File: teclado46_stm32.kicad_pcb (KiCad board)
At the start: 2 copper layers, 9 parts, among them U1 XC6206PxxxMR, U2 STM32G474CETx

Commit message: chore: add keyboard switches
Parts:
- added C14: 1u, Capacitor_SMD:C_0402_1005Metric, B.Cu at (105.9, 239.0)
- added D1: 1N4148W, Diode_SMD:D_SOD-123, B.Cu at (-143.7, 193.2)
- added D10: 1N4148W, Diode_SMD:D_SOD-123, B.Cu at (-143.7, 223.3)
- added D11: 1N4148W, Diode_SMD:D_SOD-123, B.Cu at (-149.5, 193.2)
- added D12: 1N4148W, Diode_SMD:D_SOD-123, B.Cu at (-149.5, 196.6)
- added D13: 1N4148W, Diode_SMD:D_SOD-123, B.Cu at (-149.5, 199.9)
- added D14: 1N4148W, Diode_SMD:D_SOD-123, B.Cu at (-149.5, 203.2)
- added D15: 1N4148W, Diode_SMD:D_SOD-123, B.Cu at (-149.5, 206.6)
- added D16: 1N4148W, Diode_SMD:D_SOD-123, B.Cu at (-149.5, 209.9)
- added D17: 1N4148W, Diode_SMD:D_SOD-123, B.Cu at (-149.5, 213.3)
- added D18: 1N4148W, Diode_SMD:D_SOD-123, B.Cu at (-149.5, 216.7)
- added D19: 1N4148W, Diode_SMD:D_SOD-123, B.Cu at (-149.5, 220.0)
- added D2: 1N4148W, Diode_SMD:D_SOD-123, B.Cu at (-143.7, 196.6)
- added D20: 1N4148W, Diode_SMD:D_SOD-123, B.Cu at (-149.5, 223.3)
- added D21: 1N4148W, Diode_SMD:D_SOD-123, B.Cu at (-155.3, 193.2)
- added D22: 1N4148W, Diode_SMD:D_SOD-123, B.Cu at (-155.3, 196.6)
- added D23: 1N4148W, Diode_SMD:D_SOD-123, B.Cu at (-155.3, 199.9)
- added D24: 1N4148W, Diode_SMD:D_SOD-123, B.Cu at (-155.3, 203.2)
- added D25: 1N4148W, Diode_SMD:D_SOD-123, B.Cu at (-155.3, 206.6)
- added D26: 1N4148W, Diode_SMD:D_SOD-123, B.Cu at (-155.3, 209.9)
- added D27: 1N4148W, Diode_SMD:D_SOD-123, B.Cu at (-155.3, 213.3)
- added D28: 1N4148W, Diode_SMD:D_SOD-123, B.Cu at (-155.3, 216.7)
- added D29: 1N4148W, Diode_SMD:D_SOD-123, B.Cu at (-155.3, 220.0)
- added D3: 1N4148W, Diode_SMD:D_SOD-123, B.Cu at (-143.7, 199.9)
- added D30: 1N4148W, Diode_SMD:D_SOD-123, B.Cu at (-155.3, 223.3)
- added D31: 1N4148W, Diode_SMD:D_SOD-123, B.Cu at (-161.1, 193.2)
- added D32: 1N4148W, Diode_SMD:D_SOD-123, B.Cu at (-161.1, 196.6)
- added D33: 1N4148W, Diode_SMD:D_SOD-123, B.Cu at (-161.1, 199.9)
- added D34: 1N4148W, Diode_SMD:D_SOD-123, B.Cu at (-161.1, 203.2)
- added D35: 1N4148W, Diode_SMD:D_SOD-123, B.Cu at (-161.1, 206.6)
- added D36: 1N4148W, Diode_SMD:D_SOD-123, B.Cu at (-161.1, 209.9)
- added D37: 1N4148W, Diode_SMD:D_SOD-123, B.Cu at (-161.1, 213.3)
- added D38: 1N4148W, Diode_SMD:D_SOD-123, B.Cu at (-161.1, 216.7)
- added D39: 1N4148W, Diode_SMD:D_SOD-123, B.Cu at (-161.1, 220.0)
- added D4: 1N4148W, Diode_SMD:D_SOD-123, B.Cu at (-143.7, 203.2)
- added D40: 1N4148W, Diode_SMD:D_SOD-123, B.Cu at (-161.1, 223.3)
- added D41: 1N4148W, Diode_SMD:D_SOD-123, B.Cu at (-166.9, 193.2)
- added D42: 1N4148W, Diode_SMD:D_SOD-123, B.Cu at (-166.9, 196.6)
- added D43: 1N4148W, Diode_SMD:D_SOD-123, B.Cu at (-166.9, 199.9)
- added D44: 1N4148W, Diode_SMD:D_SOD-123, B.Cu at (-166.9, 203.2)
- added D45: 1N4148W, Diode_SMD:D_SOD-123, B.Cu at (-166.9, 206.6)
- added D46: 1N4148W, Diode_SMD:D_SOD-123, B.Cu at (-166.9, 209.9)
- added D5: 1N4148W, Diode_SMD:D_SOD-123, B.Cu at (-143.7, 206.6)
- added D6: 1N4148W, Diode_SMD:D_SOD-123, B.Cu at (-143.7, 209.9)
- added D7: 1N4148W, Diode_SMD:D_SOD-123, B.Cu at (-143.7, 213.3)
- added D8: 1N4148W, Diode_SMD:D_SOD-123, B.Cu at (-143.7, 216.7)
- added D9: 1N4148W, Diode_SMD:D_SOD-123, B.Cu at (-143.7, 220.0)
- added MX1: MX_SW_HS, PCM_marbastlib-mx:SW_MX_HS_CPG151101S11_1u, B.Cu at (-45.8, 199.1)
- added MX10: MX_SW_HS, PCM_marbastlib-mx:SW_MX_HS_CPG151101S11_1u, B.Cu at (-63.0, 214.1)
- added MX11: MX_SW_HS, PCM_marbastlib-mx:SW_MX_HS_CPG151101S11_1u, B.Cu at (-63.0, 229.2)
- added MX12: MX_SW_HS, PCM_marbastlib-mx:SW_MX_HS_CPG151101S11_1u, B.Cu at (-63.0, 244.2)
- added MX13: MX_SW_HS, PCM_marbastlib-mx:SW_MX_HS_CPG151101S11_1u, B.Cu at (-63.0, 259.2)
- added MX14: MX_SW_HS, PCM_marbastlib-mx:SW_MX_HS_CPG151101S11_1u, B.Cu at (-63.0, 274.3)
- added MX15: MX_SW_HS, PCM_marbastlib-mx:SW_MX_HS_CPG151101S11_1u, B.Cu at (-63.0, 289.4)
- added MX16: MX_SW_HS, PCM_marbastlib-mx:SW_MX_HS_CPG151101S11_1u, B.Cu at (-63.0, 304.4)
- added MX17: MX_SW_HS, PCM_marbastlib-mx:SW_MX_HS_CPG151101S11_1u, B.Cu at (-80.1, 199.1)
- added MX18: MX_SW_HS, PCM_marbastlib-mx:SW_MX_HS_CPG151101S11_1u, B.Cu at (-80.1, 214.1)
- added MX19: MX_SW_HS, PCM_marbastlib-mx:SW_MX_HS_CPG151101S11_1u, B.Cu at (-80.1, 229.2)
- added MX2: MX_SW_HS, PCM_marbastlib-mx:SW_MX_HS_CPG151101S11_1u, B.Cu at (-45.8, 214.1)
- added MX20: MX_SW_HS, PCM_marbastlib-mx:SW_MX_HS_CPG151101S11_1u, B.Cu at (-80.1, 244.2)
- added MX21: MX_SW_HS, PCM_marbastlib-mx:SW_MX_HS_CPG151101S11_1u, B.Cu at (-80.1, 259.2)
- added MX22: MX_SW_HS, PCM_marbastlib-mx:SW_MX_HS_CPG151101S11_1u, B.Cu at (-80.1, 274.3)
- added MX23: MX_SW_HS, PCM_marbastlib-mx:SW_MX_HS_CPG151101S11_1u, B.Cu at (-80.1, 289.4)
- added MX24: MX_SW_HS, PCM_marbastlib-mx:SW_MX_HS_CPG151101S11_1u, B.Cu at (-80.1, 304.4)
- added MX25: MX_SW_HS, PCM_marbastlib-mx:SW_MX_HS_CPG151101S11_1u, B.Cu at (-97.3, 199.1)
- added MX26: MX_SW_HS, PCM_marbastlib-mx:SW_MX_HS_CPG151101S11_1u, B.Cu at (-97.3, 214.1)
- added MX27: MX_SW_HS, PCM_marbastlib-mx:SW_MX_HS_CPG151101S11_1u, B.Cu at (-97.3, 229.2)
- added MX28: MX_SW_HS, PCM_marbastlib-mx:SW_MX_HS_CPG151101S11_1u, B.Cu at (-97.3, 244.2)
- added MX29: MX_SW_HS, PCM_marbastlib-mx:SW_MX_HS_CPG151101S11_1u, B.Cu at (-97.3, 259.2)
- added MX3: MX_SW_HS, PCM_marbastlib-mx:SW_MX_HS_CPG151101S11_1u, B.Cu at (-45.8, 229.2)
- added MX30: MX_SW_HS, PCM_marbastlib-mx:SW_MX_HS_CPG151101S11_1u, B.Cu at (-97.3, 274.3)
- added MX31: MX_SW_HS, PCM_marbastlib-mx:SW_MX_HS_CPG151101S11_1u, B.Cu at (-97.3, 289.4)
- added MX32: MX_SW_HS, PCM_marbastlib-mx:SW_MX_HS_CPG151101S11_1u, B.Cu at (-97.3, 304.4)
- added MX33: MX_SW_HS, PCM_marbastlib-mx:SW_MX_HS_CPG151101S11_1u, B.Cu at (-114.4, 199.1)
- added MX34: MX_SW_HS, PCM_marbastlib-mx:SW_MX_HS_CPG151101S11_1u, B.Cu at (-114.4, 214.1)
- added MX35: MX_SW_HS, PCM_marbastlib-mx:SW_MX_HS_CPG151101S11_1u, B.Cu at (-114.4, 229.2)
- added MX36: MX_SW_HS, PCM_marbastlib-mx:SW_MX_HS_CPG151101S11_1u, B.Cu at (-114.4, 244.2)
- added MX37: MX_SW_HS, PCM_marbastlib-mx:SW_MX_HS_CPG151101S11_1u, B.Cu at (-114.4, 259.2)
- added MX38: MX_SW_HS, PCM_marbastlib-mx:SW_MX_HS_CPG151101S11_1u, B.Cu at (-114.4, 274.3)
- added MX39: MX_SW_HS, PCM_marbastlib-mx:SW_MX_HS_CPG151101S11_1u, B.Cu at (-114.4, 289.4)
- added MX4: MX_SW_HS, PCM_marbastlib-mx:SW_MX_HS_CPG151101S11_1u, B.Cu at (-45.8, 244.2)
- added MX40: MX_SW_HS, PCM_marbastlib-mx:SW_MX_HS_CPG151101S11_1u, B.Cu at (-114.4, 304.4)
- added MX41: MX_SW_HS, PCM_marbastlib-mx:SW_MX_HS_CPG151101S11_1u, B.Cu at (-131.6, 199.1)
- added MX42: MX_SW_HS, PCM_marbastlib-mx:SW_MX_HS_CPG151101S11_1u, B.Cu at (-131.6, 214.1)
- added MX43: MX_SW_HS, PCM_marbastlib-mx:SW_MX_HS_CPG151101S11_1u, B.Cu at (-131.6, 229.2)
- added MX44: MX_SW_HS, PCM_marbastlib-mx:SW_MX_HS_CPG151101S11_1u, B.Cu at (-131.6, 244.2)
- added MX45: MX_SW_HS, PCM_marbastlib-mx:SW_MX_HS_CPG151101S11_1u, B.Cu at (-131.6, 259.2)
- added MX46: MX_SW_HS, PCM_marbastlib-mx:SW_MX_HS_CPG151101S11_1u, B.Cu at (-131.6, 274.3)
- added MX5: MX_SW_HS, PCM_marbastlib-mx:SW_MX_HS_CPG151101S11_1u, B.Cu at (-45.8, 259.2)
- added MX6: MX_SW_HS, PCM_marbastlib-mx:SW_MX_HS_CPG151101S11_1u, B.Cu at (-45.8, 274.3)
- added MX7: MX_SW_HS, PCM_marbastlib-mx:SW_MX_HS_CPG151101S11_1u, B.Cu at (-45.8, 289.4)
- added MX8: MX_SW_HS, PCM_marbastlib-mx:SW_MX_HS_CPG151101S11_1u, B.Cu at (-45.8, 304.4)
- added MX9: MX_SW_HS, PCM_marbastlib-mx:SW_MX_HS_CPG151101S11_1u, B.Cu at (-63.0, 199.1)
- added U4: W25Q128JVS, Package_SO:SOIC-8_5.3x5.3mm_P1.27mm, B.Cu at (105.7, 230.9)
- moved C3 109.1 mm to (159.9, 247.8)
- moved U1 109.1 mm to (165.4, 231.6)
- moved C6 109.1 mm to (147.8, 238.9)
- moved C7 109.1 mm to (147.8, 240.8)
- moved U2 109.1 mm to (133.2, 223.1)
- moved C1 109.1 mm to (161.4, 230.2)
- moved C2 109.1 mm to (161.4, 232.2)
- moved C4 109.1 mm to (147.8, 234.9)
- moved C5 109.1 mm to (147.8, 236.9)
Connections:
- U2 pad 14: unconnected-(U2-PA6-Pad14) -> Q_103
- U2 pad 15: unconnected-(U2-PA7-Pad15) -> Q_102
- U2 pad 16: unconnected-(U2-PB0-Pad16) -> Q_101
- U2 pad 17: unconnected-(U2-PB1-Pad17) -> Q_100
- U2 pad 22: unconnected-(U2-PB10-Pad22) -> Q_CLK
- U2 pad 25: unconnected-(U2-PB11-Pad25) -> Q_SEL

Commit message: chore: routed caps, flash and regulator
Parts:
- moved D36 428.0 mm to (244.5, 73.0), turned to 90 degrees
- moved D46 427.9 mm to (244.5, 92.1), turned to 90 degrees
- moved D24 426.7 mm to (244.5, 54.0), turned to 90 degrees
- moved D12 425.8 mm to (244.5, 34.9), turned to 90 degrees
- moved MX46 416.4 mm to (241.3, 88.9)
- moved MX24 409.4 mm to (241.3, 50.8)
- moved D35 408.9 mm to (225.4, 73.0), turned to 90 degrees
- moved D45 408.7 mm to (225.4, 92.1), turned to 90 degrees
- moved D23 407.7 mm to (225.4, 54.0), turned to 90 degrees
- moved D11 407.0 mm to (225.4, 34.9), turned to 90 degrees
- moved D10 397.6 mm to (206.4, 34.9), turned to 90 degrees
- moved MX36 396.1 mm to (241.3, 69.8)
- moved MX45 392.7 mm to (222.2, 88.9)
- moved D34 389.8 mm to (206.4, 73.0), turned to 90 degrees
- moved D44 389.5 mm to (206.4, 92.1), turned to 90 degrees
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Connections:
- C3 pad 1: +3.3V -> +3V3
- C4 pad 1: +3.3V -> +3V3
- C5 pad 1: +3.3V -> +3V3
- C6 pad 1: +3.3V -> +3V3
- C7 pad 1: +3.3V -> +3V3
- D1 pad 1: unconnected-(D1-K-Pad1) -> ROW 0
- D10 pad 1: unconnected-(D10-K-Pad1) -> ROW 0
- D11 pad 1: unconnected-(D11-K-Pad1) -> ROW 0
- D12 pad 1: unconnected-(D12-K-Pad1) -> ROW 0
- D13 pad 1: unconnected-(D13-K-Pad1) -> ROW 1
- D14 pad 1: unconnected-(D14-K-Pad1) -> ROW 1
- D15 pad 1: unconnected-(D15-K-Pad1) -> ROW 1
- D16 pad 1: unconnected-(D16-K-Pad1) -> ROW 1
- D17 pad 1: unconnected-(D17-K-Pad1) -> ROW 1
- D18 pad 1: unconnected-(D18-K-Pad1) -> ROW 1
- D19 pad 1: unconnected-(D19-K-Pad1) -> ROW 1
- D2 pad 1: unconnected-(D2-K-Pad1) -> ROW 0
- D20 pad 1: unconnected-(D20-K-Pad1) -> ROW 1
- D21 pad 1: unconnected-(D21-K-Pad1) -> ROW 1
- D22 pad 1: unconnected-(D22-K-Pad1) -> ROW 1
- D23 pad 1: unconnected-(D23-K-Pad1) -> ROW 1
- D24 pad 1: unconnected-(D24-K-Pad1) -> ROW 1
- D25 pad 1: unconnected-(D25-K-Pad1) -> ROW 2
- D26 pad 1: unconnected-(D26-K-Pad1) -> ROW 2
- D27 pad 1: unconnected-(D27-K-Pad1) -> ROW 2
- D28 pad 1: unconnected-(D28-K-Pad1) -> ROW 2
- D29 pad 1: unconnected-(D29-K-Pad1) -> ROW 2
- D3 pad 1: unconnected-(D3-K-Pad1) -> ROW 0
- D30 pad 1: unconnected-(D30-K-Pad1) -> ROW 2
- D31 pad 1: unconnected-(D31-K-Pad1) -> ROW 2
- D32 pad 1: unconnected-(D32-K-Pad1) -> ROW 2
- D33 pad 1: unconnected-(D33-K-Pad1) -> ROW 2
- D34 pad 1: unconnected-(D34-K-Pad1) -> ROW 2
- D35 pad 1: unconnected-(D35-K-Pad1) -> ROW 2
- D36 pad 1: unconnected-(D36-K-Pad1) -> ROW 2
- D37 pad 1: unconnected-(D37-K-Pad1) -> ROW 3
- D38 pad 1: unconnected-(D38-K-Pad1) -> ROW 3
- D39 pad 1: unconnected-(D39-K-Pad1) -> ROW 3
- D4 pad 1: unconnected-(D4-K-Pad1) -> ROW 0
- D40 pad 1: unconnected-(D40-K-Pad1) -> ROW 3
- D41 pad 1: unconnected-(D41-K-Pad1) -> ROW 3
- D42 pad 1: unconnected-(D42-K-Pad1) -> ROW 3
- D43 pad 1: unconnected-(D43-K-Pad1) -> ROW 3
- D44 pad 1: unconnected-(D44-K-Pad1) -> ROW 3
- D45 pad 1: unconnected-(D45-K-Pad1) -> ROW 3
- D46 pad 1: unconnected-(D46-K-Pad1) -> ROW 3
- D5 pad 1: unconnected-(D5-K-Pad1) -> ROW 0
- D6 pad 1: unconnected-(D6-K-Pad1) -> ROW 0
- D7 pad 1: unconnected-(D7-K-Pad1) -> ROW 0
- D8 pad 1: unconnected-(D8-K-Pad1) -> ROW 0
- D9 pad 1: unconnected-(D9-K-Pad1) -> ROW 0
- MX1 pad 1: unconnected-(MX1-Pad1) -> COL 0
- MX10 pad 1: unconnected-(MX10-Pad1) -> COL 9
- MX11 pad 1: unconnected-(MX11-Pad1) -> COL 10
- MX12 pad 1: unconnected-(MX12-Pad1) -> COL 11
- MX13 pad 1: unconnected-(MX13-Pad1) -> COL 0
- MX14 pad 1: unconnected-(MX14-Pad1) -> COL 1
- MX15 pad 1: unconnected-(MX15-Pad1) -> COL 2
- MX16 pad 1: unconnected-(MX16-Pad1) -> COL 3
- MX17 pad 1: unconnected-(MX17-Pad1) -> COL 4
- MX18 pad 1: unconnected-(MX18-Pad1) -> COL 5
- MX19 pad 1: unconnected-(MX19-Pad1) -> COL 6
- MX2 pad 1: unconnected-(MX2-Pad1) -> COL 1
- MX20 pad 1: unconnected-(MX20-Pad1) -> COL 7
- MX21 pad 1: unconnected-(MX21-Pad1) -> COL 8
- MX22 pad 1: unconnected-(MX22-Pad1) -> COL 9
- MX23 pad 1: unconnected-(MX23-Pad1) -> COL 10
- MX24 pad 1: unconnected-(MX24-Pad1) -> COL 11
- MX25 pad 1: unconnected-(MX25-Pad1) -> COL 0
- MX26 pad 1: unconnected-(MX26-Pad1) -> COL 1
- MX27 pad 1: unconnected-(MX27-Pad1) -> COL 2
- MX28 pad 1: unconnected-(MX28-Pad1) -> COL 3
- MX29 pad 1: unconnected-(MX29-Pad1) -> COL 4
- MX3 pad 1: unconnected-(MX3-Pad1) -> COL 2
- MX30 pad 1: unconnected-(MX30-Pad1) -> COL 5
- MX31 pad 1: unconnected-(MX31-Pad1) -> COL 6
- MX32 pad 1: unconnected-(MX32-Pad1) -> COL 7
- MX33 pad 1: unconnected-(MX33-Pad1) -> COL 8
- MX34 pad 1: unconnected-(MX34-Pad1) -> COL 9
- MX35 pad 1: unconnected-(MX35-Pad1) -> COL 10
- MX36 pad 1: unconnected-(MX36-Pad1) -> COL 11
- MX37 pad 1: unconnected-(MX37-Pad1) -> COL 0
- MX38 pad 1: unconnected-(MX38-Pad1) -> COL 1
- MX39 pad 1: unconnected-(MX39-Pad1) -> COL 2
- MX4 pad 1: unconnected-(MX4-Pad1) -> COL 3
- MX40 pad 1: unconnected-(MX40-Pad1) -> COL 3
- MX41 pad 1: unconnected-(MX41-Pad1) -> COL 4
- MX42 pad 1: unconnected-(MX42-Pad1) -> COL 7
- MX43 pad 1: unconnected-(MX43-Pad1) -> COL 8
- MX44 pad 1: unconnected-(MX44-Pad1) -> COL 9
- MX45 pad 1: unconnected-(MX45-Pad1) -> COL 10
- MX46 pad 1: unconnected-(MX46-Pad1) -> COL 11
- MX5 pad 1: unconnected-(MX5-Pad1) -> COL 4
- MX6 pad 1: unconnected-(MX6-Pad1) -> COL 5
- MX7 pad 1: unconnected-(MX7-Pad1) -> COL 6
- MX8 pad 1: unconnected-(MX8-Pad1) -> COL 7
- MX9 pad 1: unconnected-(MX9-Pad1) -> COL 8
- U2 pad 10: unconnected-(U2-PA2-Pad10) -> Q_SEL
- U2 pad 11: unconnected-(U2-PA3-Pad11) -> Q_CLK
- U2 pad 21: +3.3V -> +3V3
- U2 pad 24: +3.3V -> +3V3
- U2 pad 36: +3.3V -> +3V3
- U2 pad 48: +3.3V -> +3V3
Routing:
- net +3V3: track 0.00 -> 44.5 mm
- net Q_CLK: track 0.00 -> 21.6 mm
- net Q_103: track 0.00 -> 19.4 mm
- net GND: track 0.00 -> 19.2 mm, vias 0 -> 8
- net Q_100: track 0.00 -> 13.4 mm
- net Q_102: track 0.00 -> 10.4 mm
- net Q_101: track 0.00 -> 9.38 mm
- net +5V: track 0.00 -> 1.68 mm
- added copper zone on B.Cu, net GND
- added copper zone on F.Cu, net GND
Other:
- board outline added: 228.6 x 76.2 mm

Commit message: chore: routed all current components
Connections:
- U2 pad 22: Q_CLK -> unconnected-(U2-PB10-Pad22)
- U2 pad 25: Q_SEL -> unconnected-(U2-PB11-Pad25)
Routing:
- net ROW 0: track 0.00 -> 361.9 mm
- net ROW 1: track 0.00 -> 323.9 mm
- net ROW 2: track 0.00 -> 323.8 mm
- net ROW 3: track 0.00 -> 250.7 mm, vias 0 -> 2
- net COL 7: track 0.00 -> 76.3 mm
- net COL 4: track 0.00 -> 75.3 mm
- net COL 0: track 0.00 -> 71.6 mm
- net COL 10: track 0.00 -> 71.5 mm
- net COL 8: track 0.00 -> 71.5 mm
- net COL 11: track 0.00 -> 71.5 mm
- net COL 2: track 0.00 -> 71.5 mm
- net COL 1: track 0.00 -> 71.5 mm
- net COL 3: track 0.00 -> 71.5 mm
- net COL 9: track 0.00 -> 71.5 mm
- net COL 6: track 0.00 -> 48.9 mm
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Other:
- outline, holes or cut-outs redrawn

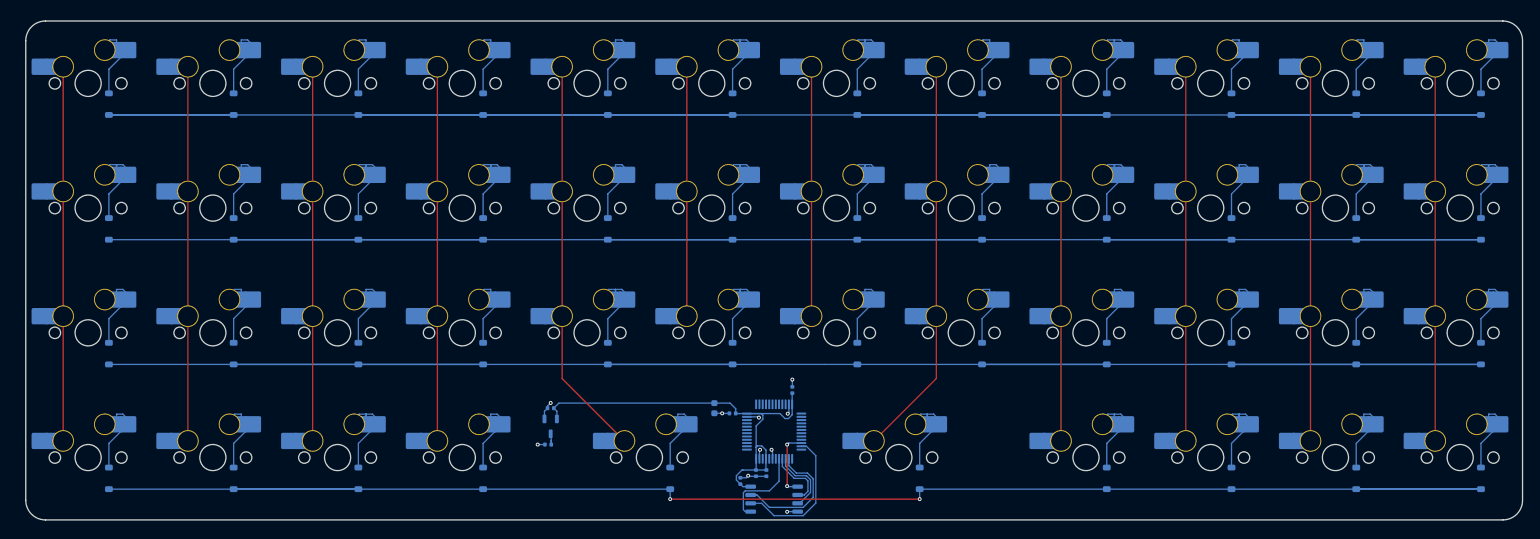
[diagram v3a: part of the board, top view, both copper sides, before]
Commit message: chore: wired udb connector
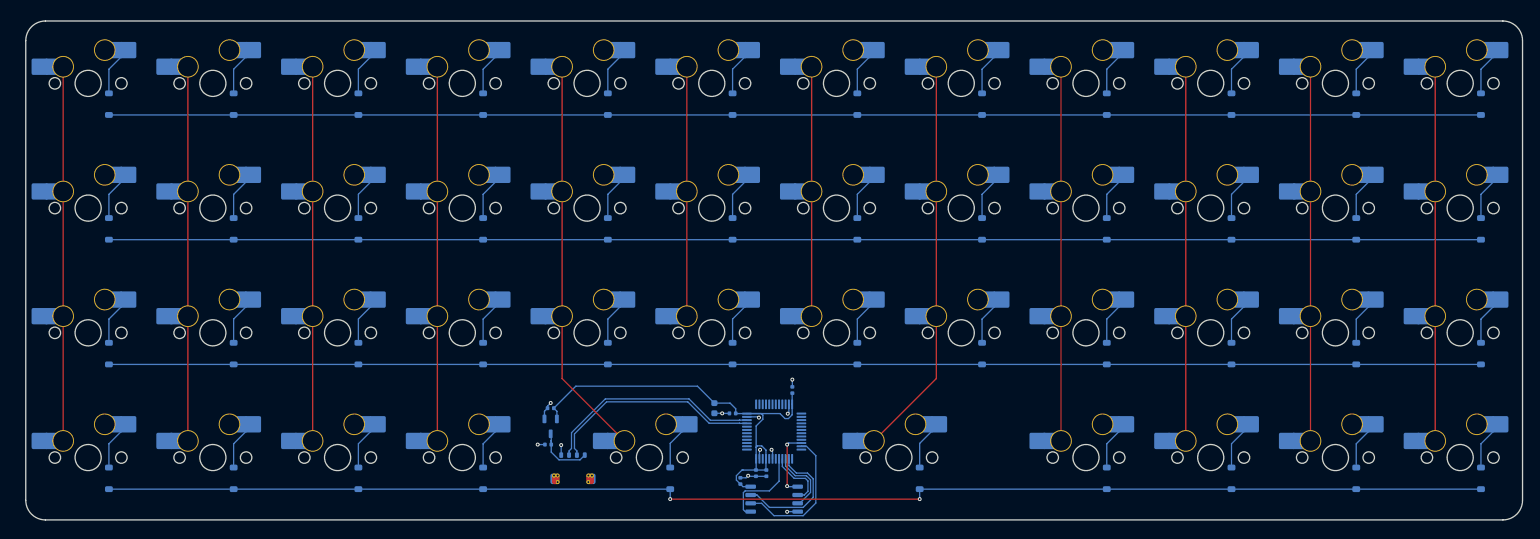
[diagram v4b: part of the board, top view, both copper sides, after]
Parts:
- added J2: 78171-0004, PCM_marbastlib-various:Molex_Pico-EZmate_78171-0004_1x04-1MP_P1.20mm_Vertical, B.Cu at (105.8, 90.4)
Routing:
- net ROW 0: track 361.9 -> 209.6 mm
- net ROW 1: track 323.9 -> 209.6 mm
- net ROW 2: track 323.8 -> 209.6 mm
- net ROW 3: track 250.7 -> 212.6 mm
- net D+: track 0.00 -> 33.9 mm
- net D-: track 0.00 -> 33.1 mm
- net COL 7: track 76.3 -> 61.1 mm
- net COL 0: track 71.6 -> 57.1 mm
- net COL 10: track 71.5 -> 57.1 mm
- net COL 8: track 71.5 -> 57.1 mm
- net COL 11: track 71.5 -> 57.1 mm
- net COL 2: track 71.5 -> 57.1 mm
- net COL 1: track 71.5 -> 57.1 mm
- net COL 3: track 71.5 -> 57.1 mm
- net COL 9: track 71.5 -> 57.1 mm
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
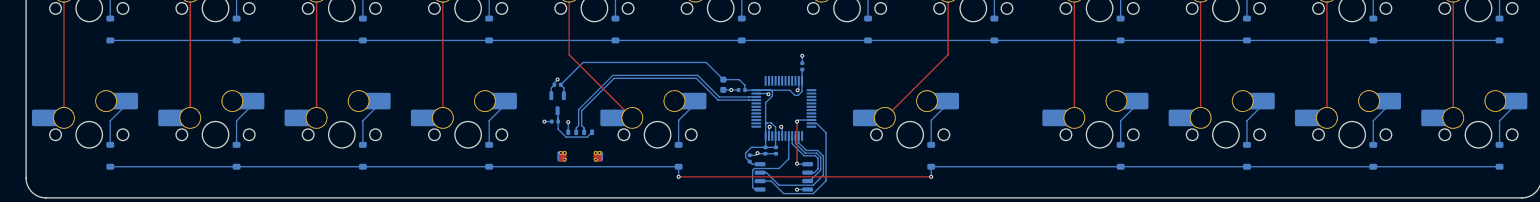
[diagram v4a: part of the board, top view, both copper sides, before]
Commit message: chore: routed columns
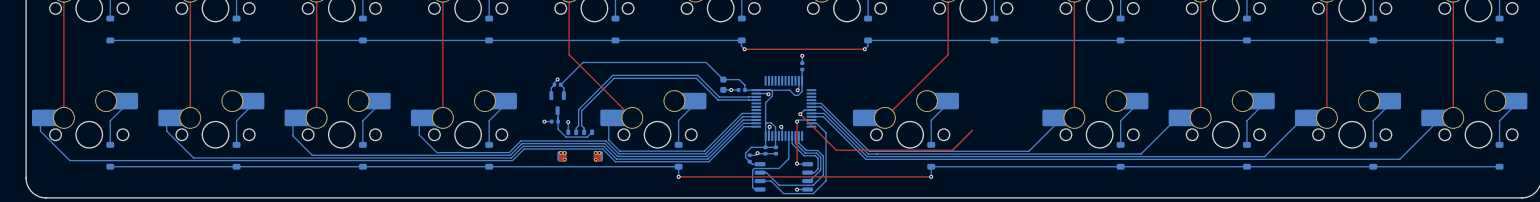
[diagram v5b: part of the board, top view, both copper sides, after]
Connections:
- U2 pad 25: unconnected-(U2-PB11-Pad25) -> COL 0
- U2 pad 26: unconnected-(U2-PB12-Pad26) -> COL 1
- U2 pad 27: unconnected-(U2-PB13-Pad27) -> COL 2
- U2 pad 28: unconnected-(U2-PB14-Pad28) -> COL 3
- U2 pad 29: unconnected-(U2-PB15-Pad29) -> COL 4
- U2 pad 5: unconnected-(U2-PF0-Pad5) -> COL 8
- U2 pad 6: unconnected-(U2-PF1-Pad6) -> COL 9
- U2 pad 8: unconnected-(U2-PA0-Pad8) -> COL 10
- U2 pad 9: unconnected-(U2-PA1-Pad9) -> COL 11
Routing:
- net COL 0: track 57.1 -> 172.7 mm
- net COL 11: track 57.1 -> 158.1 mm
- net COL 1: track 57.1 -> 153.5 mm
- net COL 10: track 57.1 -> 136.5 mm
- net COL 2: track 57.1 -> 134.8 mm
- net COL 9: track 57.1 -> 117.9 mm
- net COL 3: track 57.1 -> 115.5 mm
- net COL 8: track 57.1 -> 100.1 mm
- net NRST: track 0.00 -> 31.5 mm, vias 0 -> 1
- net COL 4: track 61.1 -> 89.7 mm
- net ROW 2: track 209.6 -> 211.7 mm, vias 0 -> 2

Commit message: chore: routed all columns
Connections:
- U2 pad 30: unconnected-(U2-PA8-Pad30) -> COL 5
- U2 pad 4: unconnected-(U2-PC15-Pad4) -> COL 7
- U2 pad 44: unconnected-(U2-PB7-Pad44) -> COL 6
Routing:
- net ROW 0: track 209.6 -> 252.8 mm, vias 0 -> 2
- net COL 5: track 38.1 -> 63.2 mm, vias 0 -> 1
- net ROW 1: track 209.6 -> 233.4 mm
- net COL 6: track 38.1 -> 52.1 mm
- net COL 7: track 61.1 -> 69.7 mm
- net ROW 2: track 211.7 -> 215.9 mm
- net GND: vias 11 -> 12

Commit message: chore: routed rows
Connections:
- U2 pad 18: unconnected-(U2-PB2-Pad18) -> ROW 3
- U2 pad 37: unconnected-(U2-PA13-Pad37) -> ROW 2
- U2 pad 42: unconnected-(U2-PB5-Pad42) -> ROW 1
- U2 pad 43: unconnected-(U2-PB6-Pad43) -> ROW 0
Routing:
- net ROW 3: track 212.6 -> 218.8 mm, vias 2 -> 3
- net ROW 2: track 215.9 -> 217.9 mm
- net ROW 1: track 233.4 -> 234.8 mm
- net ROW 0: track 252.8 -> 254.1 mm
